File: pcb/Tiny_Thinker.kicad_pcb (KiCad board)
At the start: 4 copper layers, 65 x 63.1 mm, 42 parts, among them J2 PERIPHERALS, J3 ADC_TIM, J8 USB_C_Receptacle_USB2.0_16P, SW1 SW_Push, SW2 SW_SPDT, U1 STM32F446RET6, U2 AMS1117-3.3, Y1 16MHz

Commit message: named USB connectors
idk why they keep on resetting
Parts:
- moved C7 27.3 mm to (97.0, 112.7)
- moved SW1 27.3 mm to (97.5, 109.0)
- moved R1 13.0 mm to (100.6, 97.0)
- moved SW2 13.0 mm to (96.8, 96.2)
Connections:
- D2 pad 1: Net-(D2-I/O1-Pad1) -> /USB_D-
- J8 pad A6: Net-(D2-I/O2-Pad3) -> /USB_D+
- J8 pad A7: Net-(D2-I/O1-Pad1) -> /USB_D-
- J8 pad B6: Net-(D2-I/O2-Pad3) -> /USB_D+
- J8 pad B7: Net-(D2-I/O1-Pad1) -> /USB_D-
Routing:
- net Net-(D2-I/O2-Pad3): track 5.66 -> 0.00 mm
- net /USB_D+: track 4.75 -> 10.4 mm
- net Net-(D2-I/O1-Pad1): track 4.98 -> 0.00 mm
- net /USB_D-: track 4.75 -> 9.73 mm

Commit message: i forgot to save again
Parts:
- moved FM2 87.4 mm to (97.5, 123.5)
- moved FM1 82.6 mm to (98.0, 82.2)
- moved FM3 29.1 mm to (155.0, 83.8)
- moved C3 0.28 mm to (132.7, 93.8)
- moved C6 0.28 mm to (132.7, 92.2)
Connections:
- J2 pad 10: GND -> +3.3V
- J2 pad 11: GND -> /SPI1_NSS
- J2 pad 12: GND -> /PC11
- J2 pad 13: +3.3V -> /SPI1_SCK
- J2 pad 14: +3.3V -> /PC12
- J2 pad 15: /I2C1_SCL -> /SPI1_MISO
- J2 pad 16: /I2C1_SCL -> GND
- J2 pad 17: /I2C1_SDA -> /SPI1_MOSI
- J2 pad 18: /I2C1_SDA -> +3.3V
- J2 pad 23: GND -> /I2C1_SCL
- J2 pad 24: /CAN1_RX -> /I2C1_SCL
- J2 pad 25: +3.3V -> /I2C1_SDA
- J2 pad 26: /CAN1_TX -> /I2C1_SDA
- J2 pad 3: /SPI1_NSS -> /PA15
- J2 pad 31: GND -> /SPI2_MOSI
- J2 pad 32: GND -> /CAN1_RX
- J2 pad 33: unconnected-(J2-Pin_33-Pad33) -> /SPI2_MISO
- J2 pad 34: unconnected-(J2-Pin_34-Pad34) -> /CAN1_TX
- J2 pad 35: unconnected-(J2-Pin_35-Pad35) -> /SPI2_SCK
- J2 pad 36: unconnected-(J2-Pin_36-Pad36) -> GND
- J2 pad 37: unconnected-(J2-Pin_37-Pad37) -> /SPI2_NSS
- J2 pad 38: unconnected-(J2-Pin_38-Pad38) -> +3.3V
- J2 pad 39: unconnected-(J2-Pin_39-Pad39) -> GND
- J2 pad 40: unconnected-(J2-Pin_40-Pad40) -> GND
- J2 pad 5: /SPI1_SCK -> /PC10
- J2 pad 7: /SPI1_MISO -> GND
- J2 pad 9: /SPI1_MOSI -> +3.3V
- J3 pad 1: /TIM3_CH4 -> +VBUSF
- J3 pad 12: +3.3V -> /TIM3_CH1
- J3 pad 13: /ADC1_IN9 -> +3.3V
- J3 pad 16: /ADC1_IN8 -> +3.3V
- J3 pad 17: /ADC1_IN15 -> /ADC1_IN9
- J3 pad 20: /ADC1_IN14 -> /ADC1_IN8
- J3 pad 21: +3.3V -> /ADC1_IN15
- J3 pad 24: +3.3V -> /ADC1_IN14
- J3 pad 25: /TIM2_CH4 -> +3.3V
- J3 pad 28: /TIM2_CH3 -> +3.3V
- J3 pad 29: /TIM2_CH2 -> /TIM2_CH4
- J3 pad 32: /TIM2_CH1 -> /TIM2_CH3
- J3 pad 33: unconnected-(J3-Pin_33-Pad33) -> /TIM2_CH2
- J3 pad 34: unconnected-(J3-Pin_34-Pad34) -> GND
- J3 pad 35: unconnected-(J3-Pin_35-Pad35) -> GND
- J3 pad 36: unconnected-(J3-Pin_36-Pad36) -> /TIM2_CH1
- J3 pad 37: unconnected-(J3-Pin_37-Pad37) -> +3.3V
- J3 pad 38: unconnected-(J3-Pin_38-Pad38) -> GND
- J3 pad 39: unconnected-(J3-Pin_39-Pad39) -> GND
- J3 pad 4: /TIM3_CH3 -> +VBUSF
- J3 pad 40: unconnected-(J3-Pin_40-Pad40) -> +3.3V
- J3 pad 5: /TIM3_CH2 -> /TIM3_CH4
- J3 pad 8: /TIM3_CH1 -> /TIM3_CH3
- J3 pad 9: +3.3V -> /TIM3_CH2
- U1 pad 33: unconnected-(U1-PB12-Pad33) -> /SPI2_NSS
- U1 pad 34: unconnected-(U1-PB13-Pad34) -> /SPI2_SCK
- U1 pad 35: unconnected-(U1-PB14-Pad35) -> /SPI2_MISO
- U1 pad 36: unconnected-(U1-PB15-Pad36) -> /SPI2_MOSI
- U1 pad 50: unconnected-(U1-PA15-Pad50) -> /PA15
- U1 pad 51: unconnected-(U1-PC10-Pad51) -> /PC10
- U1 pad 52: unconnected-(U1-PC11-Pad52) -> /PC11
- U1 pad 53: unconnected-(U1-PC12-Pad53) -> /PC12
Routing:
- net GND: track 79.3 -> 35.6 mm, vias 46 -> 35
- net /CAN1_TX: track 4.89 -> 34.0 mm
- net /SPI1_MOSI: track 0.00 -> 27.6 mm
- net /CAN1_RX: track 5.09 -> 32.1 mm
- net /SPI1_MISO: track 0.00 -> 26.5 mm
- net /SPI1_SCK: track 0.00 -> 25.7 mm
- net /PA15: track 0.00 -> 25.6 mm
- net /PC10: track 0.00 -> 24.9 mm
- net /SPI1_NSS: track 0.00 -> 24.8 mm
- net /I2C1_SDA: track 2.43 -> 26.2 mm
- net +VBUSF: track 6.65 -> 28.9 mm
- net /I2C1_SCL: track 2.18 -> 23.5 mm
- net /SWDIO: track 5.86 -> 26.0 mm
- net /PC12: track 0.00 -> 19.2 mm
- net /PC11: track 0.00 -> 19.1 mm
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
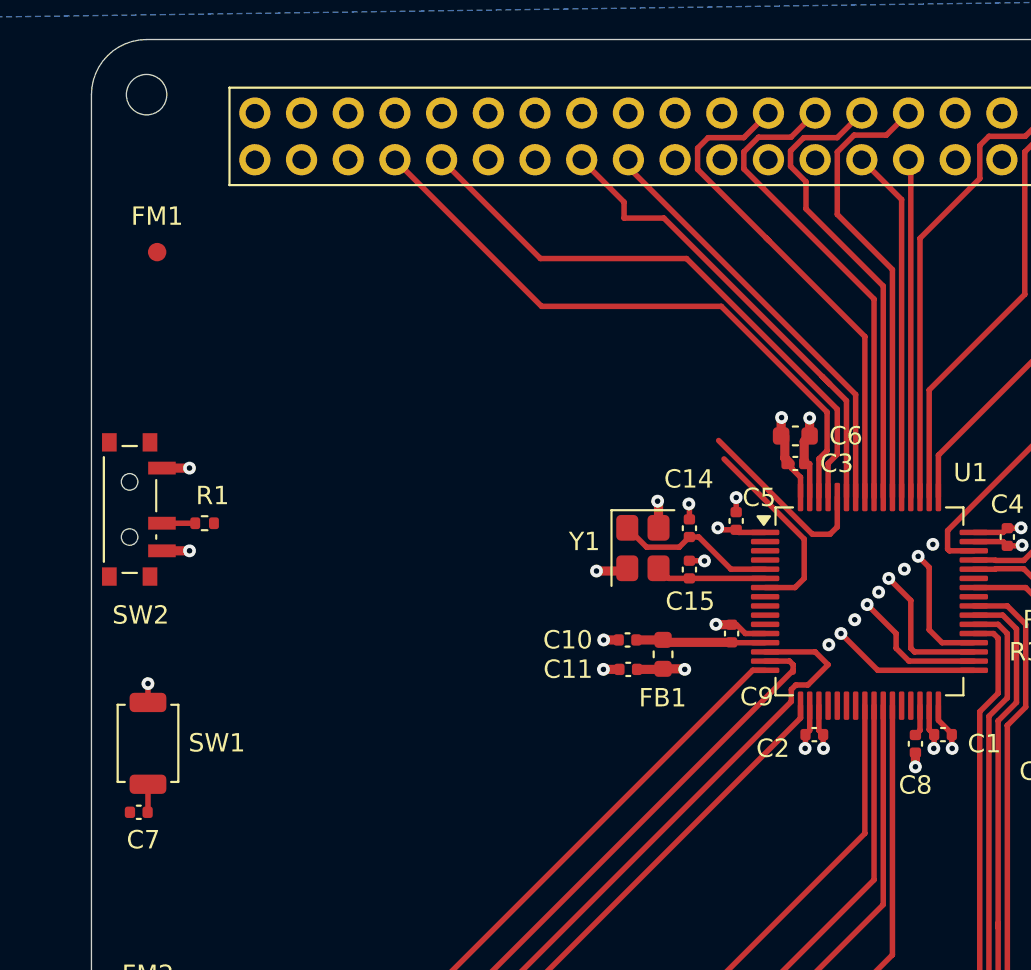
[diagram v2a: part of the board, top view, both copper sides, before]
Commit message: added misc pins
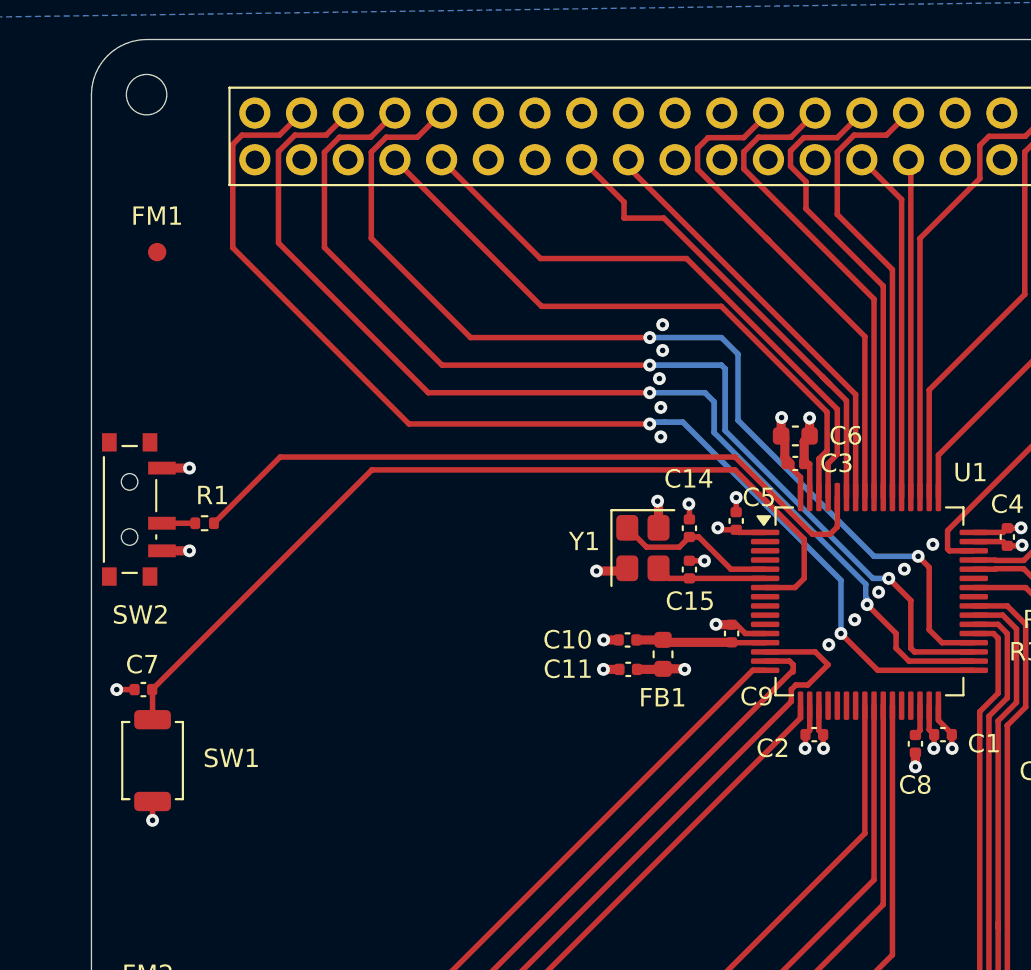
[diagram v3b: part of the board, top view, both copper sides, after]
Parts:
- moved C7 6.68 mm to (97.2, 106.0)
- moved SW1 0.97 mm to (97.8, 109.9), turned to -90 degrees
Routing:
- net /SPI2_NSS: track 8.05 -> 61.7 mm, vias 1 -> 2
- net /SPI2_SCK: track 7.58 -> 59.0 mm, vias 1 -> 2
- net /SPI2_MISO: track 7.80 -> 57.8 mm, vias 1 -> 2
- net /SPI2_MOSI: track 6.96 -> 55.4 mm, vias 1 -> 2
- net /NRST: track 12.1 -> 48.0 mm
- net /BOOT0: track 10.4 -> 38.9 mm
- net GND: track 35.6 -> 36.6 mm, vias 35 -> 41

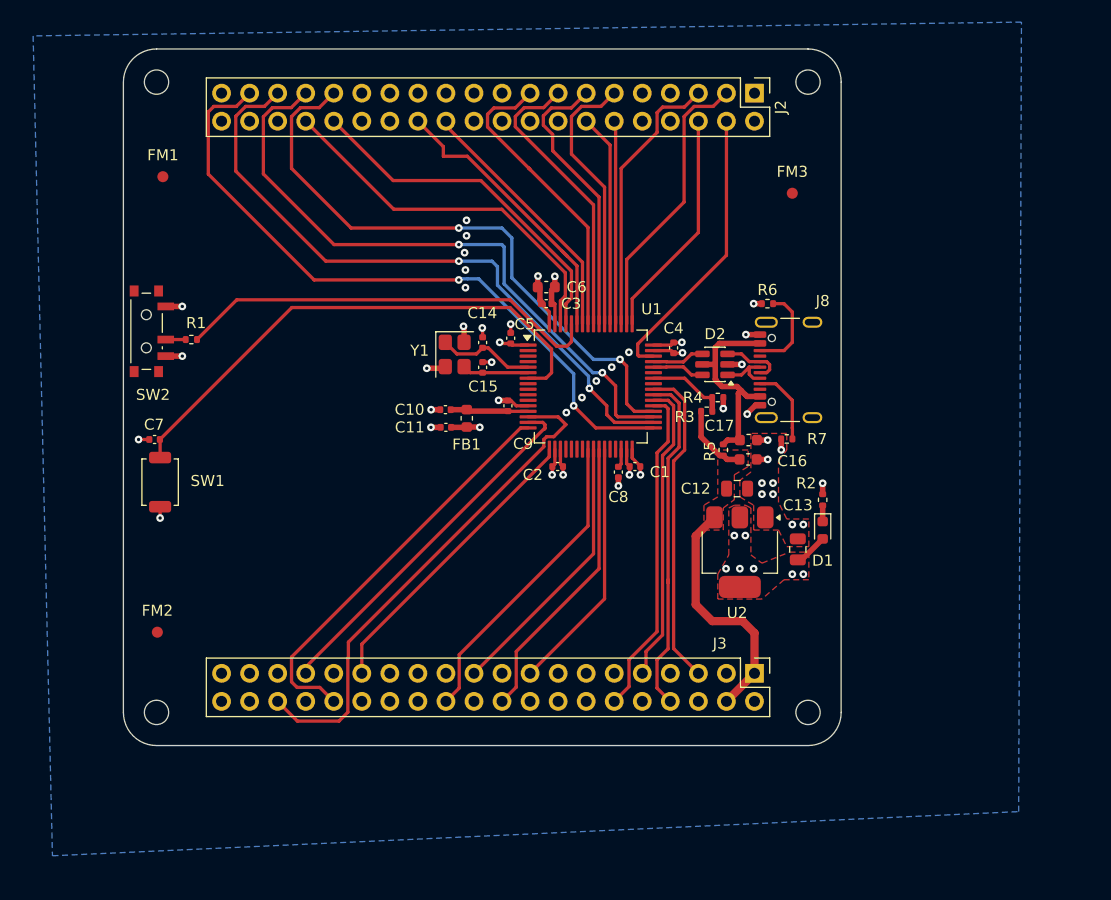
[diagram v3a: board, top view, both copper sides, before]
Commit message: added ground pour to L1
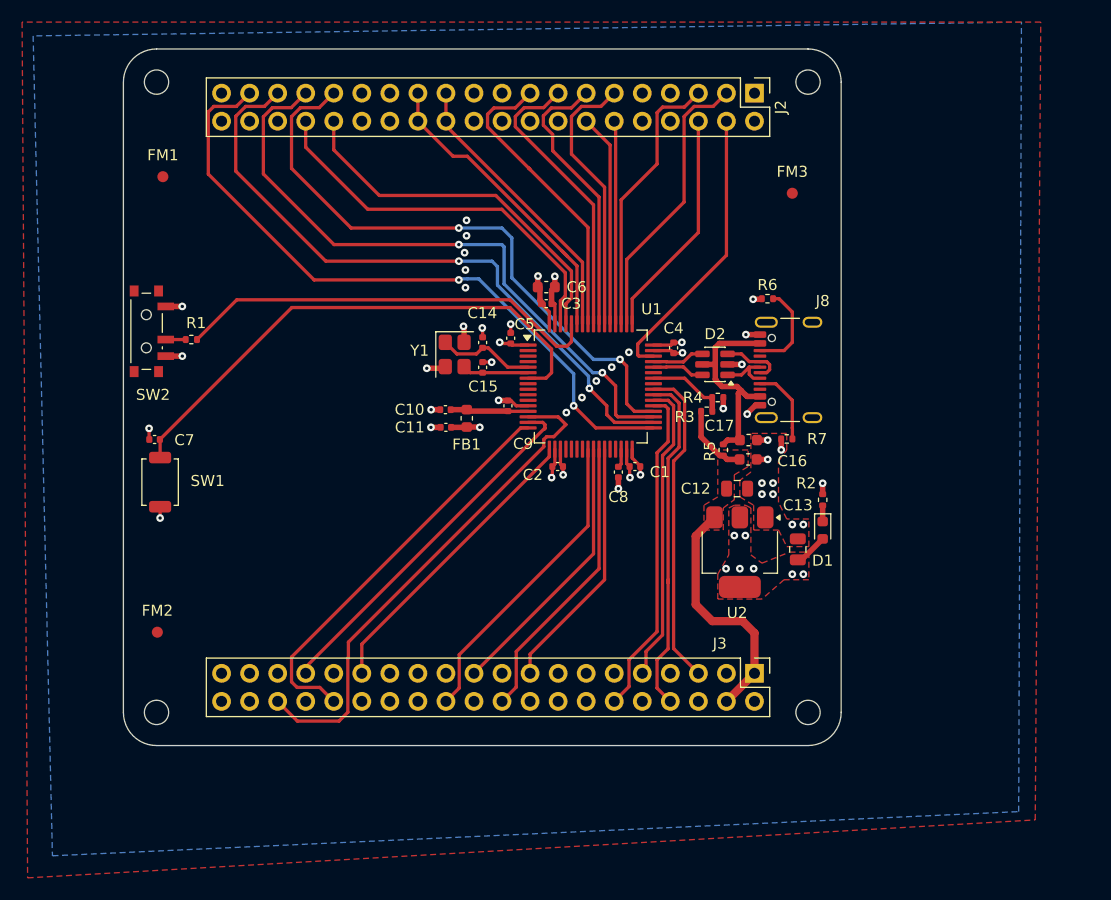
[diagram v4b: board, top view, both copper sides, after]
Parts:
- moved R6 0.45 mm to (152.8, 93.3)
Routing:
- net /I2C1_SCL: track 23.5 -> 26.0 mm
- net /I2C1_SDA: track 26.2 -> 28.2 mm
- net /CAN1_RX: track 32.1 -> 33.7 mm
- net /CAN1_TX: track 34.0 -> 35.4 mm
- net GND: track 36.6 -> 37.3 mm
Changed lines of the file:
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@@
 	(footprint "Resistor_SMD:R_0402_1005Metric"
 		(layer "F.Cu")
-		(at 152.75 93.75 180)
+		(at 152.75 93.3 180)
 		(descr "Resistor SMD 0402 (1005 Metric), square (rectangular) end terminal, IPC-7351 nominal, (Body size source: IPC-SM-782 page 72, https://www.pcb-3d.com/wordpress/wp-content/uploads/ipc-sm-782a_amendment_1_and_2.pdf), generated with kicad-footprint-generator")
 		(tags "resistor")
@@
 		(tags "capacitor")
 		(property "Reference" "C7"
-			(at 0.05 1.35 0)
+			(at -2.7 -0.05 0)
 			(layer "F.SilkS")
 			(effects
@@
 		(stroke
 			(width 0.1)
-			(type default)
+			(type dash)
 		)
 		(layer "Dwgs.User")
@@
 		(stroke
 			(width 0.1)
-			(type solid)
+			(type dash)
 		)
 		(layer "Dwgs.User")
@@
 	)
 	(segment
-		(start 139.25 109.48)
-		(end 139.25 110.25)
-		(width 0.5)
-		(layer "F.Cu")
-		(net 1)
-	)
-	(segment
 		(start 123.45 99.6)
 		(end 121.9 99.6)
@@
 	)
 	(segment
+		(start 140.27 109.27)
+		(end 140.27 108.5)
+		(width 0.3)
+		(layer "F.Cu")
+		(net 1)
+	)
+	(segment
 		(start 133.2 93.75)
 		(end 133.2 92.545)
@@
 	)
 	(segment
-		(start 140.27 109.27)
-		(end 140.25 109.25)
+		(start 140.3 109.3)
+		(end 140.27 109.27)
 		(width 0.3)
 		(layer "F.Cu")
@@
 	)
 	(segment
-		(start 149.1375 99.25)
-		(end 150.5 99.25)
+		(start 139.25 110.5)
+		(end 139.25 109.48)
 		(width 0.5)
 		(layer "F.Cu")
@@
 	)
 	(segment
-		(start 142.425 98)
-		(end 144.02 98)
-		(width 0.3)
+		(start 149.1375 99.25)
+		(end 150.5 99.25)
+		(width 0.5)
 		(layer "F.Cu")
 		(net 1)
 	)
 	(segment
-		(start 140.27 109.27)
-		(end 140.27 108.5)
+		(start 142.425 98)
+		(end 144.02 98)
 		(width 0.3)
 		(layer "F.Cu")
@@
 	)
 	(segment
-		(start 96.77 106.05)
-		(end 95.8 106.05)
+		(start 96.75 106.02)
+		(end 96.75 105.05)
 		(width 0.3)
 		(layer "F.Cu")
@@
 	)
 	(segment
-		(start 152.24 93.75)
-		(end 151.5 93.75)
+		(start 152.19 93.35)
+		(end 151.45 93.35)
 		(width 0.5)
 		(layer "F.Cu")
@@
 	)
 	(segment
+		(start 140.3 109.5)
+		(end 140.3 109.3)
+		(width 0.3)
+		(layer "F.Cu")
+		(net 1)
+	)
+	(segment
+		(start 133.2 109.3)
+		(end 133.27 109.23)
+		(width 0.3)
+		(layer "F.Cu")
+		(net 1)
+	)
+	(segment
 		(start 126.955 96.79)
 		(end 126.955 95.98)
@@
 	)
 	(segment
-		(start 133.27 109.23)
-		(end 133.25 109.25)
+		(start 133.2 109.5)
+		(end 133.2 109.3)
 		(width 0.3)
 		(layer "F.Cu")
@@
 	)
 	(segment
-		(start 133.27 108.5)
-		(end 133.27 109.23)
+		(start 133.27 109.23)
+		(end 133.27 108.5)
 		(width 0.3)
 		(layer "F.Cu")
@@
 	)
 	(via
-		(at 133.25 109.25)
+		(at 133.2 109.5)
 		(size 0.7)
 		(drill 0.3)
@@
 	)
 	(via
-		(at 139.25 110.25)
+		(at 139.25 110.5)
 		(size 0.7)
 		(drill 0.3)
@@
 	)
 	(via
-		(at 140.25 109.25)
+		(at 140.3 109.5)
 		(size 0.7)
 		(drill 0.3)
@@
 	)
 	(via
-		(at 95.8 106.05)
+		(at 96.75 105.05)
 		(size 0.7)
 		(drill 0.3)
@@
 	)
 	(via
-		(at 151.5 93.75)
+		(at 151.45 93.35)
 		(size 0.7)
 		(drill 0.3)
@@
 	)
 	(segment
-		(start 134.6 89.432959)
-		(end 134.183521 89.016479)
+		(start 123.635 77.225)
+		(end 123.635 74.685)
 		(width 0.3)
 		(layer "F.Cu")
-		(net 13)
+		(net 12)
 	)
 	(segment
-		(start 123.4 80.4)
-		(end 123.4 79.53)
+		(start 134.6 89.432959)
+		(end 134.183521 89.016479)
 		(width 0.3)
 		(layer "F.Cu")
@@
 	)
 	(segment
-		(start 123.4 79.53)
-		(end 121.095 77.225)
+		(start 121.095 77.225)
+		(end 121.095 74.685)
 		(width 0.3)
 		(layer "F.Cu")
@@
 	)
 	(segment
-		(start 125.567041 80.4)
-		(end 123.4 80.4)
+		(start 134.183521 89.016479)
+		(end 125.567041 80.4)
 		(width 0.3)
 		(layer "F.Cu")
@@
 	)
 	(segment
-		(start 134.183521 89.016479)
-		(end 125.567041 80.4)
+		(start 124.27 80.4)
+		(end 121.095 77.225)
+		(width 0.3)
+		(layer "F.Cu")
+		(net 13)
+	)
+	(segment
+		(start 125.567041 80.4)
+		(end 124.27 80.4)
 		(width 0.3)
 		(layer "F.Cu")
@@
 	(segment
 		(start 135 90.8)
-		(end 126.8 82.6)
+		(end 128.15 83.95)
 		(width 0.3)
 		(layer "F.Cu")
@@
 	)
 	(segment
-		(start 135 93.25)
-		(end 135 90.8)
+		(start 128.15 83.95)
+		(end 117.6 83.95)
 		(width 0.3)
 		(layer "F.Cu")
@@
 	)
 	(segment
-		(start 118.85 82.6)
+		(start 113.475 79.825)
 		(end 113.475 77.225)
 		(width 0.3)
@@
 	)
 	(segment
+		(start 117.6 83.95)
+		(end 113.475 79.825)
+		(width 0.3)
+		(layer "F.Cu")
+		(net 33)
+	)
+	(segment
 		(start 134.5 95.575)
 		(end 134.5 93.75)
@@
 	)
 	(segment
-		(start 134.5 93.75)
-		(end 135 93.25)
+		(start 135 93.25)
+		(end 135 90.8)
 		(width 0.3)
 		(layer "F.Cu")
@@
 	)
 	(segment
-		(start 126.8 82.6)
-		(end 118.85 82.6)
+		(start 134.5 93.75)
+		(end 135 93.25)
 		(width 0.3)
 		(layer "F.Cu")
@@
 	)
 	(segment
+		(start 138 118.75)
+		(end 131.255 125.495)
+		(width 0.3)
+		(layer "F.Cu")
+		(net 35)
+	)
+	(segment
 		(start 138 106.925)
-		(end 138 120.48)
+		(end 138 118.75)
 		(width 0.3)
 		(layer "F.Cu")
@@
 	)
 	(segment
-		(start 138 120.48)
+		(start 131.255 125.495)
 		(end 131.255 127.225)
 		(width 0.3)
@@
 	)
 	(segment
-		(start 134 95.575)
-		(end 134 93.5)
+		(start 128.691364 85.2)
+		(end 116.55 85.2)
 		(width 0.3)
 		(layer "F.Cu")
@@
 	)
 	(segment
-		(start 134.445682 90.954318)
-		(end 128.691364 85.2)
+		(start 116.55 85.2)
+		(end 110.935 79.585)
 		(width 0.3)
 		(layer "F.Cu")
@@
 	)
 	(segment
+		(start 110.935 79.585)
+		(end 110.935 77.225)
+		(width 0.3)
+		(layer "F.Cu")
+		(net 40)
+	)
+	(segment
 		(start 134 93.5)
 		(end 134.445682 93.054318)
@@
 	)
 	(segment
-		(start 128.691364 85.2)
-		(end 118.91 85.2)
+		(start 134.445682 90.954318)
+		(end 128.691364 85.2)
 		(width 0.3)
 		(layer "F.Cu")
@@
 	)
 	(segment
-		(start 118.91 85.2)
-		(end 110.935 77.225)
+		(start 134 95.575)
+		(end 134 93.5)
 		(width 0.3)
 		(layer "F.Cu")
@@
 	)
 	(segment
-		(start 152.07 98)
-		(end 154.25 98)
+		(start 153.8 93.3)
+		(end 153.26 93.3)
 		(width 0.3)
 		(layer "F.Cu")
@@
 	)
 	(segment
-		(start 154.25 98)
-		(end 155 97.25)
+		(start 155 94.5)
+		(end 153.8 93.3)
 		(width 0.3)
 		(layer "F.Cu")
@@
 	)
 	(segment
-		(start 155 94.5)
-		(end 154.25 93.75)
+		(start 155 97.25)
+		(end 155 94.5)
 		(width 0.3)
 		(layer "F.Cu")
@@
 	)
 	(segment
-		(start 155 97.25)
-		(end 155 94.5)
+		(start 152.07 98)
+		(end 154.25 98)
 		(width 0.3)
 		(layer "F.Cu")
@@
 	)
 	(segment
-		(start 154.25 93.75)
-		(end 153.26 93.75)
+		(start 154.25 98)
+		(end 155 97.25)
 		(width 0.3)
 		(layer "F.Cu")
@@
 	)
 	(segment
-		(start 139.5 81.5)
-		(end 142.754 78.246)
+		(start 143.25 75.95)
+		(end 145.23 75.95)
 		(width 0.3)
 		(layer "F.Cu")
@@
 	)
 	(segment
-		(start 142.754 78.246)
-		(end 142.754 76.446)
+		(start 139.5 84.35)
+		(end 142.754 81.096)
 		(width 0.3)
 		(layer "F.Cu")
@@
 	)
 	(segment
-		(start 145.23 75.95)
-		(end 146.495 74.685)
+		(start 142.754 81.096)
+		(end 142.754 76.446)
 		(width 0.3)
 		(layer "F.Cu")
@@
 	(segment
 		(start 139.5 95.575)
-		(end 139.5 81.5)
+		(end 139.5 84.35)
 		(width 0.3)
 		(layer "F.Cu")
@@
 	)
 	(segment
-		(start 143.25 75.95)
-		(end 145.23 75.95)
+		(start 145.23 75.95)
+		(end 146.495 74.685)
 		(width 0.3)
 		(layer "F.Cu")
@@
 	)
 	(zone
-		(net 2)
-		(net_name "+3.3V")
-		(layer "B.Cu")
+		(net 1)
+		(net_name "GND")
+		(layers "F.Cu" "In1.Cu" "In2.Cu")
 		(name "L2_L3_GND")
 		(hatch edge 0.5)
@@
 		(polygon
 			(pts
-				(xy 88 143.75) (xy 175.5 139.75) (xy 175.75 68.25) (xy 86.25 69.5)
+				(xy 85.75 145.75) (xy 177 140.5) (xy 177.5 68.25) (xy 85.25 68.25)
 			)
 		)
 	)
 	(zone
-		(net 1)
-		(net_name "GND")
-		(layers "In1.Cu" "In2.Cu")
+		(net 2)
+		(net_name "+3.3V")
+		(layer "B.Cu")
 		(name "L2_L3_GND")
 		(hatch edge 0.5)
@@
 		(polygon
 			(pts
-				(xy 85.75 145.75) (xy 177 140.5) (xy 177.5 68.25) (xy 85.25 68.25)
+				(xy 88 143.75) (xy 175.5 139.75) (xy 175.75 68.25) (xy 86.25 69.5)
 			)
 		)
